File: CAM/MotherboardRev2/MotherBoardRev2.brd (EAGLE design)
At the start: 160 x 100 mm, 229 parts, among them IC1 DRV8814, IC2 DRV8814, IC3 PIC24FJ64GB202, IC4 PIC24FJ256GB106, Q1 BSS123, Q2 BSS123, Q3 BSS123, U1 LMS8117AMP-3.3, U2 DRV8811PWP, U3 LMS8117AMP-3.3, U4 DRV8811PWP

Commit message: Done with Motherboard
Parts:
- added C71: 0.1uF, rcl:C0402
- added MOTIN5: 22-05-7048-04, Son_of_Dark_Power:7395-04
- R10, R11: value (none) -> 10K
- R13: value 470 -> 100
- R19, R20: value 4.7k -> 10K
- R21, R22, R23, R24, R25: value (none) -> 330
- R67, R68, R69, R70, R71: value (none) -> 1K
- moved C38 5.74 mm to (75.0, 85.5), turned to 180 degrees
- moved R54 4.26 mm to (55.6, 93.9)
- moved R64 4.26 mm to (55.6, 93.9)
- moved LED3 4.24 mm to (55.6, 96.6)
- moved LED13 4.22 mm to (55.6, 96.5)
- moved C56 0.90 mm to (23.9, 87.8)
- moved C26 0.89 mm to (76.0, 49.6)
- moved SERVO_1 0.09 mm to (152.4, 78.2), flipped to the bottom, turned to 270 degrees
- flipped SERVO_2 to the bottom, turned to 270 degrees
- flipped 3.3V to the bottom
- flipped 3.3V(2) to the bottom
- flipped 3.3V(2)1 to the bottom
- flipped 3.3V1 to the bottom
- flipped 5V to the bottom
- flipped 5V(2) to the bottom
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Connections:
- removed net AVDD: IC4.19
- removed net AVSS: IC4.20
- net +7V: now also MOTIN5.2, MOTIN5.3
- net 3.3V: now also C71.1, IC4.19
- net GND: now also C71.2, IC4.20, MOTIN5.1, MOTIN5.4
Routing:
- net VOUT5: track 71.2 -> 49.7 mm
- net OC5: track 108.5 -> 117.9 mm
- net OC1: track 65.6 -> 73.8 mm
- net OC6: track 124.3 -> 129.8 mm
- net +7V: track 72.4 -> 77.7 mm
- net OC2: track 81.5 -> 86.6 mm
- net 3.3V: track 361.7 -> 366.5 mm
- net OC3: track 90.0 -> 94.7 mm
- net OC4: track 98.2 -> 102.9 mm

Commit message: Added values for some of the capactiors
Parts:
- removed Q1, Q2, Q3: BSS123, transistor-small-signal:SOT23
- added C72: 4.7uF, rcl:C0402
- added LED14: (no value), led:CHIP-LED0603
- added LIDAR: (no value), con-lstb:MA04-1
- added R65: 10k, rcl:R0402
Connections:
- removed net EN1: Q2.1
- removed net EN2: Q1.1
- removed net EN3: Q3.1
- removed net ENA_1: Q2.3, U$2.5
- removed net ENA_2: Q1.3, U$4.5
- removed net ENA_3: Q3.3, U$8.5
- new net N$19: LED14.A, R65.1
- new net UART_RX: LIDAR.2, U$1.P9.22
- new net UART_TX: LIDAR.3, U$1.P9.21
- net 3.3V: now also C72.1, LIDAR.4
- net GND: now also C72.2, LED14.C, LIDAR.1; no longer Q1.2, Q2.2, Q3.2
- net VCC: now also R65.2
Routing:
- net 3.3V: track 366.5 -> 414.6 mm
- net UART_RX: track 0.00 -> 33.2 mm
- net UART_TX: track 0.00 -> 32.7 mm
- net OC3: track 94.7 -> 86.9 mm
- net GND: track 197.5 -> 190.2 mm
- net ENA_3: track 6.25 -> 0.00 mm, vias 1 -> 0
- net ENA_1: track 6.25 -> 0.00 mm, vias 1 -> 0
- net ENA_2: track 6.25 -> 0.00 mm, vias 1 -> 0
- net OC2: track 86.6 -> 80.6 mm
- net OC4: track 102.9 -> 97.0 mm
- net OC5: track 117.9 -> 112.2 mm
- net OC6: track 129.8 -> 124.3 mm
- net OC1: track 73.8 -> 71.8 mm
- net VCC: track 16.7 -> 18.2 mm, vias 5 -> 6
- net N$19: track 0.01 -> 1.39 mm
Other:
- board text added: "GND"
- board text added: "Gnd"

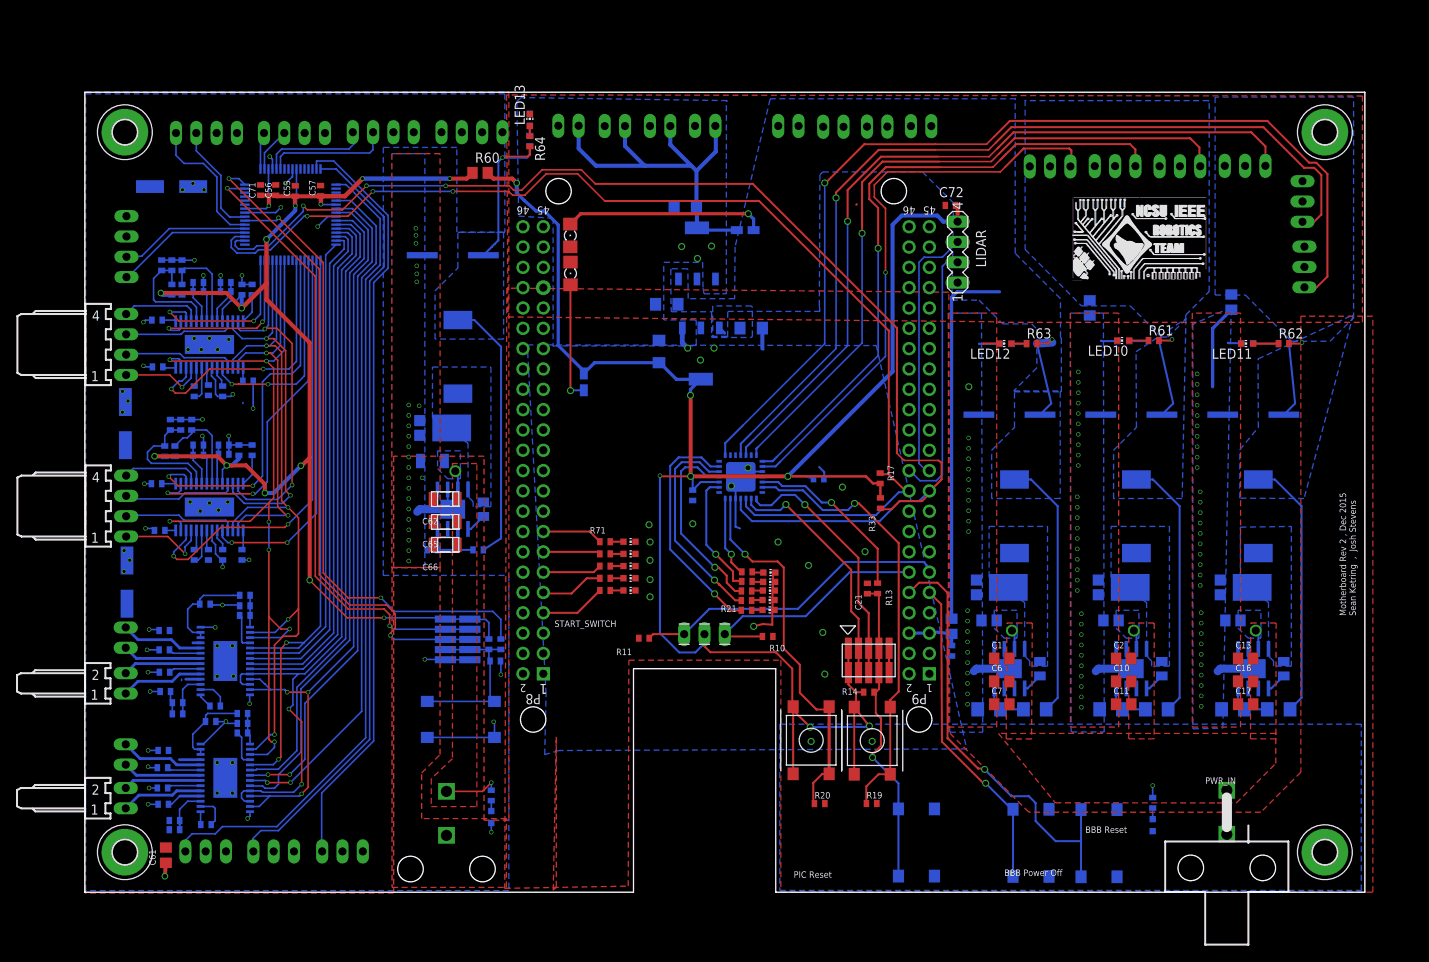
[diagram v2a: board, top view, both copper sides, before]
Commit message: ADD rplider board
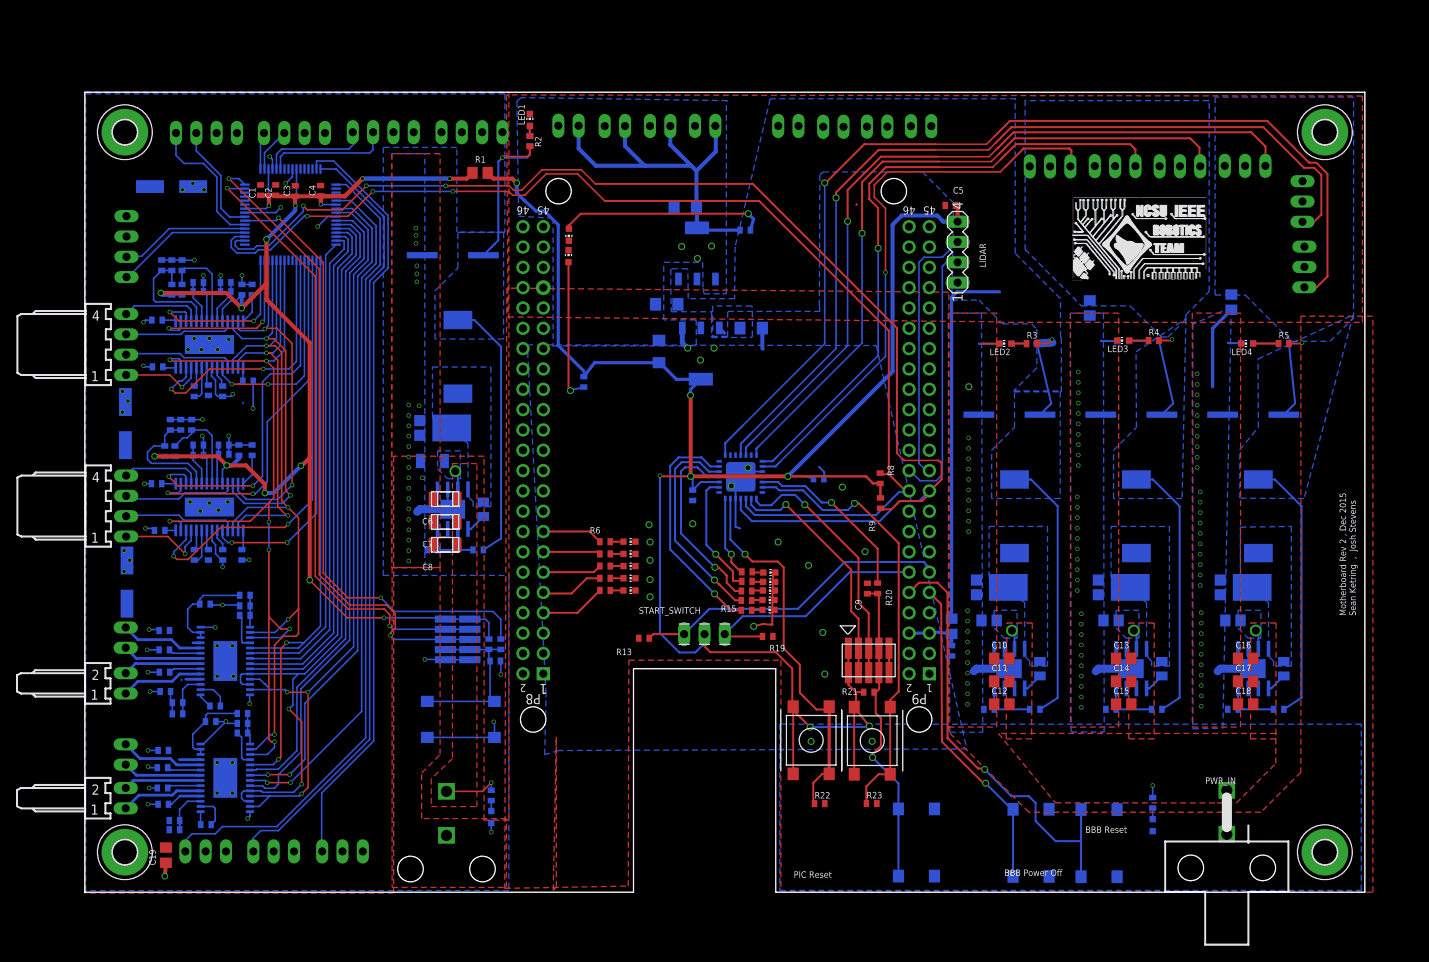
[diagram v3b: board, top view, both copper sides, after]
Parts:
- removed C21: .1uF, rcl:C0402
- removed C55: 1uF, rcl:C0402
- removed C56, C57, C71: 0.1uF, rcl:C0402
- removed C61: 10uF, rcl:C0805
- removed C62, C65, C66: 4.7uF, 5v:1206
- removed C72: 4.7uF, rcl:C0402
- removed D5, D7: 3_3V_PWR, SparkFun-LED:FKIT-LED-1206
- removed LED16, LED17, LED18, LED19, LED20: (no value), led:CHIP-LED0603
- removed MOTOR4: 22-05-7028-02, Son_of_Dark_Power:7395-02
- removed R24, R25: 330, rcl:R0402
- removed R33: 4.7K, rcl:R0402
- removed R34: (no value), rcl:R0805W
- removed R60: (no value), rcl:R0805
- removed R64: 10k, rcl:R0402
- removed R67, R68, R69, R70, R71: 1K, rcl:R0402
- removed U$10, U$11: LOGO, logo:LOGO
- removed U$6: Switch1, Parts4Class:MC32882_FINAL
- removed U$7: Switch2, Parts4Class:MC32882_FINAL
- added C104: 0.01uF, rcl:C0402
- added C108, C110, C112: 10nF, 5v:0805
- added C109, C111, C113: 4.7uF, rcl:C0805
- added C125, C126, C127: 330uF, 5v:SM_RADIAL_10AMM
- added D101, D102: PDS760-13, 5v:POWERDI5
- added LED100, LED101, LED102, LED103, LED104: (no value), led:CHIP-LED0603
- added MOTOR101: 22-05-7028-02, Son_of_Dark_Power:7395-02
- added R104, R106, R108: 10k, rcl:R0402
- added R105, R107: 2.55k, rcl:R0402
- added R109: 3.23K, rcl:R0402
- added R113: 1M, rcl:R0402
- added R121, R122: 0.2, rcl:R0402
- added R136, R138: 330, rcl:R0402
- added U$102: Switch3, Parts4Class:MC32882_FINAL
- added U$105, U$106, U$107: TPS5450DDAR, 5v:R-PDSO-G8
- C1, C2: value 4.7uF -> 0.1uF; device rcl:C0805 -> rcl:C0402
- C124, C135, C152: value (none) -> 100uf
- C14: value 10nF -> 4.7uF; device 5v:0805 -> rcl:C0805
- C15: value 330uF -> 4.7uF; device 5v:SM_RADIAL_10AMM -> rcl:C0805
- C19: value 0.01uF -> 10uF; device rcl:C0402 -> rcl:C0805
- C3: value 10nF -> 1uF; device 5v:0805 -> rcl:C0402
- C4: value 10nF -> 0.1uF; device 5v:0805 -> rcl:C0402
- C5: value 330uF -> 4.7uF; device 5v:SM_RADIAL_10AMM -> rcl:C0402
- C6, C7, C8: device rcl:C0805 -> 5v:1206
- C9: value 330uF -> .1uF; device 5v:SM_RADIAL_10AMM -> rcl:C0402
- D1, D2: value PDS760-13 -> 3_3V_PWR; device 5v:POWERDI5 -> led:CHIP-LED0603
- R1: value 10k -> 0; device rcl:R1206 -> rcl:R0805
- R10, R11: value 10K -> 1K
- R12: value 1M -> 1K
- R124: value (none) -> 2.55k
- R13: value 100 -> 10K
- R14: value 10k -> 330
- R15: value (none) -> 330; device rcl:R0805W -> rcl:R0402
- R16, R18: value 0.2 -> 330
- R17: value 4.7K -> 330
- R2: device rcl:R1206 -> rcl:R0402
- R20: value 10K -> 100
- R21: value 330 -> 10k
- R22, R23: value 330 -> 10K
- R3, R5: value (none) -> 10k; device rcl:R1206 -> rcl:R0402
- R6: value 10k -> 1K
- R7: value 10k -> 1K; device rcl:R1206 -> rcl:R0402
- R8: value (none) -> 4.7K; device rcl:R1206 -> rcl:R0402
- R9: value 10k -> 4.7K
- U$1: value BEAGLE_BONE_BLACK_CAPE -> LOGO; device Son_of_Dark_Powersch:BEAGLE_BONE_BLACK_CAPE -> logo:LOGO
- U$2: value TPS5450DDAR -> LOGO; device 5v:R-PDSO-G8 -> logo:LOGO
- U$3: value TPS5450DDAR -> Switch2; device 5v:R-PDSO-G8 -> Parts4Class:MC32882_FINAL
- U$4: value TPS5450DDAR -> Switch1; device 5v:R-PDSO-G8 -> Parts4Class:MC32882_FINAL
- U$5: value Switch3 -> BEAGLE_BONE_BLACK_CAPE; device Parts4Class:MC32882_FINAL -> Son_of_Dark_Powersch:BEAGLE_BONE_BLACK_CAPE
- moved H2 174.9 mm to (155.0, 95.0)
- moved H4 174.9 mm to (155.0, 5.00)
- moved H1 150.0 mm to (5.00, 95.0)
- moved H3 150.0 mm to (5.00, 5.00)
- moved C3 123.7 mm to (26.3, 87.6), flipped to the top
- moved C2 121.1 mm to (23.9, 87.8), turned to 90 degrees
- moved C1 109.6 mm to (22.0, 87.8), turned to 90 degrees
- moved C4 108.0 mm to (29.5, 87.7), flipped to the top
- moved R1 107.9 mm to (49.4, 89.9), flipped to the top, turned to 0 degrees
- moved R2 95.0 mm to (55.6, 93.9), flipped to the top, turned to 270 degrees
- moved R7 86.4 mm to (65.0, 42.3), flipped to the top
- moved D1 81.9 mm to (60.5, 82.2), flipped to the top, turned to 180 degrees
- moved LED1 79.1 mm to (55.6, 96.5), flipped to the top, turned to 0 degrees
- moved LED3 79.1 mm to (129.8, 69.0), flipped to the top, turned to 90 degrees
- moved U$1 77.4 mm to (130.6, 80.9), turned to 0 degrees
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- renumbered C20 to C105, C22 to C100, C23 to C136, C24 to C137, C25 to C128, C26 to C129, C27 to C143, C28 to C144, C29 to C145, C30 to C101, C31 to C149, C32 to C148, C33 to C150, C34 to C141, C35 to C139, C36 to C140, C37 to C114, C38 to C151, C39 to C133, C40 to C132, C41 to C134, C42 to C122, C43 to C120, C44 to C121, C45 to C119, C46 to C123, C47 to C142, C48 to C138, C49 to C147, C50 to C131, C51 to C106, C52 to C117, C53 to C107, C54 to C102, C58 to C152, C59 to C135, C60 to C124, C63 to C118, C64 to C146, C67 to C130, C68 to C115, C69 to C116, C70 to C103, D3 to D100, D4 to D103, IC1 to IC101, IC2 to IC100, IC3 to IC102, IC4 to IC103, L1 to L102, L2 to L101, L3 to L100, L4 to L103, MOTIN1 to MOTIN100, MOTIN2 to MOTIN102, MOTIN3 to MOTIN103, MOTIN4 to MOTIN104, MOTIN5 to MOTIN101, MOTOR3 to MOTOR100, PROGRAMMING1 to PROGRAMMING100, R26 to R118, R27 to R120, R28 to R102, R29 to R103, R30 to R114, R31 to R111, R32 to R115, R35 to R112, R36 to R137, R37 to R139, R38 to R141, R39 to R140, R40 to R144, R41 to R145, R42 to R143, R43 to R142, R44 to R132, R45 to R125, R46 to R127, R47 to R126, R48 to R131, R49 to R129, R50 to R128, R51 to R130, R52 to R123, R53 to R124, R54 to R146, R55 to R116, R56 to R117, R57 to R119, R58 to R110, R59 to R101, R61 to R134, R62 to R133, R63 to R135, R65 to R100, SERVO_1 to SERVO_103, SERVO_2 to SERVO_104, SERVO_3 to SERVO_105, SERVO_4 to SERVO_106, SERVO_5 to SERVO_107, SERVO_6 to SERVO_108, SERVO_7 to SERVO_102, SERVO_8 to SERVO_101, SERVO_9 to SERVO_100, U$12 to U$108, U$13 to U$101, U$14 to U$100, U$8 to U$104, U$9 to U$103, U1 to U103, U2 to U102, U3 to U101, U4 to U100
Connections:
- net +7V: now also C19.1, H1.B3,0, R113.2, R2.2; no longer C61.1, H4.B3,0, R12.2, R64.2
- net 3.3V: now also C1.1, C2.1, C3.1, C4.1, C5.1, R1.1, R1.2, R136.1, R21.2, R8.2, R9.2, U$3.P$1, U$3.P$4, U$4.P$1, U$4.P$4; no longer C55.1, C56.1, C57.1, C71.1, C72.1, R14.2, R15.1, R17.2, R33.2, R60.1, R60.2, U$6.P$1, U$6.P$4, U$7.P$1, U$7.P$4
- net BB_PWR_BUTTON: now also U$5.P9.9; no longer U$1.P9.9
- net BB_SYS_RESET: now also U$5.P9.10; no longer U$1.P9.10
- net BOOT1: now also C112.1, U$106.1; no longer C4.1, U$2.1
- net BOOT2: now also C110.1, U$105.1; no longer C3.1, U$4.1
- net BOOT3: now also C108.1; no longer C14.1
- net BOOT_VM: now also U$107.1; no longer U$3.1
- net GND: now also C1.2, C109.1, C111.1, C113.1, C125.2, C126.2, C127.2, C14.1, C15.1, C19.2, C2.2, C3.2, C4.2, D1.C, D101.1, D102.1, D2.C, LED100.C, LED101.C, LED102.C, LED103.C, LED104.C, R105.1, R107.1, R109.1, R121.2, R122.2, R13.1, R19.1, R22.2, R23.2, U$102.P$1, U$102.P$4, U$105.6, U$105.9, U$106.6, U$106.9, U$107.6, U$107.9, U$5.P8.1, U$5.P8.2, U$5.P9.1, U$5.P9.2, U$5.P9.43, U$5.P9.44, U$5.P9.45, U$5.P9.46; no longer C1.1, C15.2, C2.1, C21.2, C55.2, C56.2, C57.2, C61.2, C62.1, C65.1, C66.1, C71.2, C72.2, D1.1, D2.1, D5.C, D7.C, LED16.C, LED17.C, LED18.C, LED19.C, LED20.C, R10.1, R11.1, R16.2, R18.2, R19.2, R20.2, R3.1, R5.1, R8.1, U$1.P8.1, U$1.P8.2, U$1.P9.1, U$1.P9.2, U$1.P9.43, U$1.P9.44, U$1.P9.45, U$1.P9.46, U$2.6, U$2.9, U$3.6, U$3.9, U$4.6, U$4.9, U$5.P$1, U$5.P$4
- net GPIO23: now also R7.2, U$5.P8.13; no longer R70.2, U$1.P8.13
- net GPIO45: now also R10.2, U$5.P8.11; no longer R69.2, U$1.P8.11
- net GPIO47: now also R6.2, U$5.P8.15; no longer R71.2, U$1.P8.15
- net GPIO66: now also R12.2, U$5.P8.7; no longer R67.2, U$1.P8.7
- net GPIO69: now also R11.2, U$5.P8.9; no longer R68.2, U$1.P8.9
- net IO3: now also R18.2; no longer R25.2
- net IO4: now also R17.2; no longer R24.2
- net IO5: now also R16.2; no longer R23.2
- net IO6: now also R14.2; no longer R22.2
- net IO7: now also R15.2; no longer R21.2
- net M1-MAOUT1: now also MOTOR1.1; no longer MOTOR2.1
- net M1-MAOUT2: now also MOTOR1.2; no longer MOTOR2.2
- net M1-MBOUT1: now also MOTOR101.1; no longer MOTOR1.1
- net M1-MBOUT2: now also MOTOR101.2; no longer MOTOR1.2
- net M2-MAOUT1: now also MOTOR2.1; no longer MOTOR4.1
- net M2-MAOUT2: now also MOTOR2.2; no longer MOTOR4.2
- net MCLR: now also C9.1, R20.2, R21.1, U$102.P$2, U$102.P$3; no longer C21.1, R13.2, R14.1, U$5.P$2, U$5.P$3
- net MCLR': now also R20.1; no longer R13.1
- net N$1: now also LED103.A, R135.1; no longer LED4.A, R4.1
- net N$10: now also D2.A, R136.2; no longer D5.A, R15.2
- net N$11: now also D1.A, R138.2; no longer D7.A, R34.2
- net N$12: now also C104.1; no longer C19.1
- net N$13: now also R113.1; no longer R12.1
- net N$14: now also R121.1; no longer R16.1
- net N$15: now also R122.1; no longer R18.1
- net N$18: now also U$5.P9.5, U$5.P9.6; no longer U$1.P9.5, U$1.P9.6
- net N$19: now also LED100.A; no longer LED14.A
- net N$2: now also LED102.A, R134.1; no longer LED1.A, R6.1
- net N$3: now also LED101.A, R133.1; no longer LED2.A, R9.1
- net N$4: now also C104.2; no longer C19.2
- net N$5: now also LED10.A, R15.1; no longer LED5.A, R21.1
- net N$51: now also LED104.A; no longer LED3.A
- net N$55: now also LED9.A, R12.1; no longer LED16.A, R67.1
- net N$56: now also LED8.A, R11.1; no longer LED17.A, R68.1
- net N$57: now also LED7.A, R10.1; no longer LED18.A, R69.1
- net N$58: now also LED6.A, R7.1; no longer LED19.A, R70.1
- net N$59: now also LED5.A, R6.1; no longer LED20.A, R71.1
- net N$6: now also LED11.A, R14.1; no longer LED6.A, R22.1
- net N$60: now also LED3.A, R4.1; no longer LED10.A, R134.1
- net N$61: now also LED4.A, R5.1; no longer LED11.A, R133.1
- net N$62: now also LED2.A, R3.1; no longer LED12.A, R135.1
- net N$63: now also LED1.A, R2.1; no longer LED13.A, R64.1
- net N$7: now also LED12.A, R16.1; no longer LED7.A, R23.1
- net N$8: now also LED13.A, R17.1; no longer LED8.A, R24.1
- net N$9: now also LED14.A, R18.1; no longer LED9.A, R25.1
- net PH1: now also C112.2, D102.3, U$106.8; no longer C4.2, D2.3, U$2.8
- net PH2: now also C110.2, D101.3, U$105.8; no longer C3.2, D1.3, U$4.8
- net PH3: now also C108.2; no longer C14.2
- net PH_VM: now also U$107.8; no longer U$3.8
- net SCL: now also R9.1, U$5.P9.19; no longer R33.1, U$1.P9.19
- net SDA: now also R8.1, U$5.P9.20; no longer R17.1, U$1.P9.20
- net START_LEFT: now also R19.2, U$5.P9.12; no longer R10.2, U$1.P9.12
- net START_RIGHT: now also R13.2, U$5.P9.11; no longer R11.2, U$1.P9.11
- net SWITCH_1: now also R23.1, U$4.P$2, U$4.P$3; no longer R19.1, U$6.P$2, U$6.P$3
- net SWITCH_2: now also R22.1, U$3.P$2, U$3.P$3; no longer R20.1, U$7.P$2, U$7.P$3
- net UART_RX: now also U$5.P9.22; no longer U$1.P9.22
- net UART_TX: now also U$5.P9.21; no longer U$1.P9.21
- net VCC: now also C109.2, C111.2, C113.2, C14.2, C15.2, U$105.7, U$106.7, U$107.7; no longer C1.2, C2.2, C62.2, C65.2, C66.2, U$2.7, U$3.7, U$4.7
- net VOUT1: now also C127.1, R108.2, R3.2; no longer C5.1, R2.2, R4.2
- net VOUT2: now also C126.1, R106.2, R4.2; no longer C9.1, R1.2, R6.2
- net VOUT3: now also C125.1, R104.2, R5.2; no longer C15.1, R7.2, R9.2
- net VOUT5: now also R138.1; no longer R34.1
- net VSNS1: now also R108.1, R109.2, U$106.4; no longer R2.1, R3.2, U$2.4
- net VSNS2: now also R106.1, R107.2, U$105.4; no longer R1.1, R5.2, U$4.4
- net VSNS3: now also R104.1, R105.2; no longer R7.1, R8.2
- net VSNS_VM: now also U$107.4; no longer U$3.4
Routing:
- net N$10: track 14.9 -> 17.9 mm
- net VSNS2: track 5.81 -> 7.03 mm
- net VSNS1: track 5.81 -> 7.03 mm
- net VSNS3: track 5.81 -> 7.03 mm
- net 3.3V: track 414.6 -> 415.3 mm
- net N$11: track 25.1 -> 25.8 mm
- net VOUT2: track 44.5 -> 45.1 mm
- net VOUT1: track 93.8 -> 94.5 mm
- net VOUT3: track 44.0 -> 44.6 mm
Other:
- board text removed: "GND"
- board text removed: "Gnd"
